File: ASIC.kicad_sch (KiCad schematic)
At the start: 66 parts, among them U10 BM1370_mode1, U11 MCP1824T-1202E/OT, U12 MCP1824T-0802E, U2 SN74AVC4T774, U8 25MHz, U9 BM1370_mode1

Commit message: lots of routing
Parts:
- removed U11: MCP1824T-1202E/OT, Package_TO_SOT_SMD:SOT-23-5, symbol bitaxe:MCP1824
- removed U12: MCP1824T-0802E, Package_TO_SOT_SMD:SOT-23-5, symbol bitaxe:MCP1824
- added R41: 38.3k, Resistor_SMD:R_0402_1005Metric, symbol Device:R_Small_US
- added R42, R44: 20k, Resistor_SMD:R_0402_1005Metric, symbol Device:R_Small_US
- added R43: 19.1k, Resistor_SMD:R_0402_1005Metric, symbol Device:R_Small_US
- added U11, U12: MCP1824, Package_TO_SOT_SMD:SOT-23-5, symbol bitaxe:MCP1824-ADJ
- A1: renamed from U9; value BM1370_mode1 -> BM1340_mode1; footprint bitaxe:BM1370 -> bitaxe:BM1340; symbol bitaxe:BM1370_mode1 -> bitaxe:BM1340_mode1
- A2: renamed from U10; value BM1370_mode1 -> BM1340_mode1; footprint bitaxe:BM1370 -> bitaxe:BM1340; symbol bitaxe:BM1370_mode1 -> bitaxe:BM1340_mode1
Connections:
- net 0V8: now also R43.2, U12.5 (VOUT)
- net 1V2: now also R41.2, U11.5 (VOUT)
- net 5V: now also U11.1 (VIN), U11.3 (EN), U12.1 (VIN), U12.3 (EN)
- net GND: now also R42.1, R44.1, U11.2 (GND), U12.2 (GND)
- new net: R41.1, R42.2, U11.4 (ADJ)
- new net: R43.1, R44.2, U12.4 (ADJ)
- no-connect marks 3 -> 1
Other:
- title: bitaxeGamma Turbo -> bitaxeNaja
- moved on the sheet: C89, C91, TP18, TP19

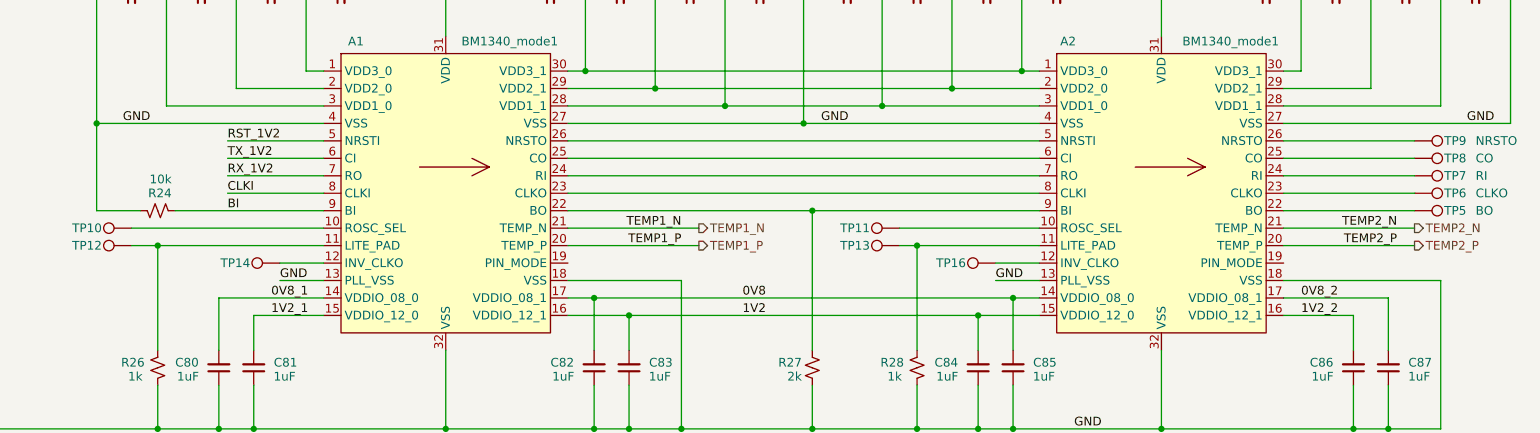
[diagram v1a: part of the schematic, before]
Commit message: placed and routed and DRC'd. updated TPS546 for 1.0V output.
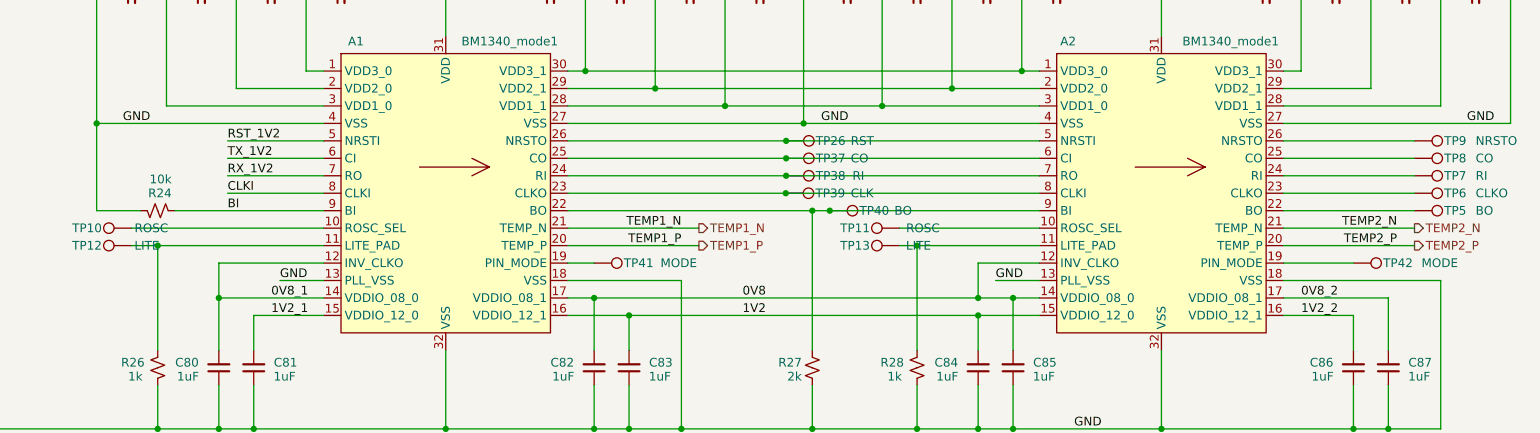
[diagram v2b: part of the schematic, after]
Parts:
- removed TP14, TP16: TestPoint, TestPoint:TestPoint_Pad_D1.0mm, symbol Connector:TestPoint
- added TP26: RST, bitaxe:TestPoint_Pad_1.0x0.4mm, symbol Connector:TestPoint
- added TP37: CO, bitaxe:TestPoint_Pad_1.0x0.4mm, symbol Connector:TestPoint
- added TP38: RI, bitaxe:TestPoint_Pad_1.0x0.4mm, symbol Connector:TestPoint
- added TP39: CLK, bitaxe:TestPoint_Pad_1.0x0.4mm, symbol Connector:TestPoint
- added TP40: BO, bitaxe:TestPoint_Pad_1.0x0.4mm, symbol Connector:TestPoint
- added TP41, TP42: MODE, bitaxe:TestPoint_Pad_1.0x0.4mm, symbol Connector:TestPoint
- R41: DK (none) -> YAG3141CT-ND; PARTNO (none) -> RC0402FR-0738K3L
- R42, R44: DK (none) -> 311-20.0KLRCT-ND; PARTNO (none) -> RC0402FR-0720KL
- R43: DK (none) -> 311-19.1KLRCT-ND; PARTNO (none) -> RC0402FR-0719K1L
- TP10, TP11: value TestPoint -> ROSC; footprint TestPoint:TestPoint_Pad_D1.0mm -> bitaxe:TestPoint_Pad_1.0x0.4mm
- TP12, TP13: value TestPoint -> LITE; footprint TestPoint:TestPoint_Pad_D1.0mm -> bitaxe:TestPoint_Pad_1.0x0.4mm
- TP5, TP6, TP7, TP8, TP9: footprint TestPoint:TestPoint_Pad_D1.0mm -> bitaxe:TestPoint_Pad_1.0x0.4mm
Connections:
- net 0V8: now also A2.12 (INV_CLKO)
- net 0V8_1: now also A1.12 (INV_CLKO)
- net at A1.19 (PIN_MODE): now also TP41.1
- net at A1.22 (BO), A2.9 (BI), R27.2: now also TP40.1
- net at A1.23 (CLKO), A2.8 (CLKI): now also TP39.1
- net at A1.24 (RI), A2.7 (RO): now also TP38.1
- net at A1.25 (CO), A2.6 (CI): now also TP37.1
- net at A1.26 (NRSTO), A2.5 (NRSTI): now also TP26.1
- net at A2.19 (PIN_MODE): now also TP42.1

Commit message: update to KiCad 10
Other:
- company: (none) -> bitaxeorg

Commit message: switched to single phase TPS546D24 and put the ASICs in series.
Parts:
- removed R41: 38.3k, Resistor_SMD:R_0402_1005Metric, symbol Device:R_Small_US
- removed R42, R44: 20k, Resistor_SMD:R_0402_1005Metric, symbol Device:R_Small_US
- removed R43: 19.1k, Resistor_SMD:R_0402_1005Metric, symbol Device:R_Small_US
- removed TP37: CO, bitaxe:TestPoint_Pad_1.0x0.4mm, symbol Connector:TestPoint
- removed TP38: RI, bitaxe:TestPoint_Pad_1.0x0.4mm, symbol Connector:TestPoint
- removed TP39: CLK, bitaxe:TestPoint_Pad_1.0x0.4mm, symbol Connector:TestPoint
- removed TP40: BO, bitaxe:TestPoint_Pad_1.0x0.4mm, symbol Connector:TestPoint
- removed U11, U12: MCP1824, Package_TO_SOT_SMD:SOT-23-5, symbol bitaxe:MCP1824-ADJ
- added C63, C96, C97, C98: 1uF, Capacitor_SMD:C_0402_1005Metric, symbol Device:C_Small
- added R38: 1k, Resistor_SMD:R_0402_1005Metric, symbol Device:R_Small_US
- added TP17: BO, bitaxe:TestPoint_Pad_1.0x0.4mm, symbol Connector:TestPoint
- added TP22: CO, bitaxe:TestPoint_Pad_1.0x0.4mm, symbol Connector:TestPoint
- added TP23: NRSTO, bitaxe:TestPoint_Pad_1.0x0.4mm, symbol Connector:TestPoint
- added TP24, TP27: GND, bitaxe:TestPoint_Pad_D1.0mm, symbol Connector:TestPoint
- added TP25, TP28: 0V8, bitaxe:TestPoint_Pad_D1.0mm, symbol Connector:TestPoint
- added TP30: 1V2, bitaxe:TestPoint_Pad_D1.0mm, symbol Connector:TestPoint
- added U10, U12: TLV77308PDBVR, Package_TO_SOT_SMD:SOT-23-5, symbol Regulator_Linear:TLV73312PDBV
- added U11, U14: TLV77312PDBVR, Package_TO_SOT_SMD:SOT-23-5, symbol Regulator_Linear:TLV73312PDBV
- A2: symbol bitaxe:BM1340_mode1 -> bitaxe:BM1340_mode0
- C88, C89, C90, C91: LCSC (none) -> C52923
- TP18: value 1V2 -> CLKO; footprint TestPoint:TestPoint_Pad_D1.5mm -> bitaxe:TestPoint_Pad_1.0x0.4mm
- TP19: value 0V8 -> RI; footprint TestPoint:TestPoint_Pad_D1.5mm -> bitaxe:TestPoint_Pad_1.0x0.4mm
- TP26: value RST -> 1V2; footprint bitaxe:TestPoint_Pad_1.0x0.4mm -> bitaxe:TestPoint_Pad_D1.0mm
- TP5: value BO -> BI
- TP6: value CLKO -> CLKI
- TP7: value RI -> RO
- TP8: value CO -> CI
- TP9: value NRSTO -> NRSTI
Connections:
- net 0V8_2 is gone; now on net 0V8_1: A2.17 (VDDIO_08_1), C87.2
- net 1V2_2 is gone; now on net 1V2_1: A2.16 (VDDIO_12_1), C86.2
- net 0V8_1: now also C97.2, TP28.1, U12.5 (OUT); no longer A1.12 (INV_CLKO), A1.14 (VDDIO_08_0), C80.2
- net 1V2: no longer A1.16 (VDDIO_12_1), A2.15 (VDDIO_12_0), C51.1, C53.1, C83.2, C84.2, C89.2, TP18.1, U2.16 (VCCA), U8.1 (EN), U8.4 (VIN)
- net 1V2_1: now also C98.2, R38.2, TP30.1, U14.5 (OUT); no longer A1.15 (VDDIO_12_0), C81.2
- net 5V: no longer C88.2, C90.2
- net GND: now also C63.1, TP24.1, U10.2 (GND), U11.2 (GND); no longer A1.27 (VSS), A2.13 (PLL_VSS), A2.18 (VSS), A2.27 (VSS), A2.32 (VSS), A2.4 (VSS), C58.2, C59.2, C60.2, C61.2, C62.2, C71.2, C72.1, C79.2, C84.1, C85.1, C86.1, C87.1, C91.1, R28.1
- net Level Shifter/BI: now reaches A1.22 (BO), R27.2
- net Level Shifter/BI: now also TP17.1; no longer A2.9 (BI)
- net at A2.8 (CO): no longer A1.23 (CLKO)
- net at A2.7 (RI): now also R38.1; no longer A1.24 (RI)
- net at A2.6 (CLKO): no longer A1.25 (CO)
- net at A1.28 (VDD1_1), C70.2, C71.1: no longer A2.3 (VDD1_0), C72.2, C73.1
- net at A1.29 (VDD2_1), C69.2, C70.1: no longer A2.2 (VDD2_0), C73.2, C74.1
- net at A1.30 (VDD3_1), C68.2, C69.1: no longer A2.1 (VDD3_0), C74.2, C75.1
- net Level Shifter/BO: now reaches TP5.1
- net Level Shifter/BO: now also A2.26 (BI); no longer A2.22 (BO)
- net Level Shifter/CLKO: now reaches TP6.1
- net Level Shifter/CLKO: now also A2.25 (CLKI); no longer A2.23 (CLKO)
- net Level Shifter/CO: now reaches TP8.1
- net Level Shifter/CO: now also A2.23 (CI); no longer A2.25 (CO)
- net GND_1: now reaches A2.19 (PIN_MODE), TP42.1
- net GND_1: now also A1.31 (VDD), A2.13 (PLL_VSS), A2.18 (VSS), A2.27 (VSS), A2.32 (VSS), A2.4 (VSS), C38.1, C54.1, C55.1, C56.1, C57.1, C58.2, C59.2, C60.2, C61.2, C62.2, C67.2, C68.1, C72.1, C79.2, C84.1, C85.1, C86.1, C87.1, C91.1, R28.1, C96.1, C97.1, C98.1, TP27.1, U12.2 (GND), U14.2 (GND)
- net Level Shifter/RI: now reaches A2.24 (RO), TP7.1
- net Level Shifter/NRSTO: now reaches TP9.1
- net Level Shifter/NRSTO: now also A2.22 (NRSTI); no longer A2.26 (NRSTO)
- removed net 0V8: A1.17 (VDDIO_08_1), A2.12 (INV_CLKO), A2.14 (VDDIO_08_0), C82.2, C85.2, C91.2, TP19.1
- net Vcore renamed VDD
- net VDD: no longer A1.31 (VDD), C38.1, C54.1, C55.1, C56.1, C57.1, C67.2, C68.1
- new net: A1.27 (VSS), C71.2
- new net: A2.3 (VDD1_0), C72.2, C73.1
- new net: A2.2 (VDD2_0), C73.2, C74.1
- new net: A2.1 (VDD3_0), C74.2, C75.1
- new net: A2.15 (VDDIO_12_0), C84.2
- new net: A2.12 (INV_CLKO), A2.14 (VDDIO_08_0), C85.2
- new net 0V8_0: A1.12 (INV_CLKO), A1.14 (VDDIO_08_0), A1.17 (VDDIO_08_1), C80.2, C82.2, C89.2, TP25.1, U10.5 (OUT)
- new net 1V2_0: A1.15 (VDDIO_12_0), A1.16 (VDDIO_12_1), C51.1, C53.1, C81.2, C83.2, C90.2, TP26.1, U11.5 (OUT), U2.16 (VCCA), U8.1 (EN), U8.4 (VIN)
- new net 5V_SWITCH: C63.2, C88.2, C91.2, C96.2, U10.1 (IN), U10.3 (EN), U11.1 (IN), U11.3 (EN), U12.1 (IN), U12.3 (EN), U14.1 (IN), U14.3 (EN)
- new net Level Shifter/CI: A1.25 (CO), TP22.1
- new net Level Shifter/CLKI: A1.23 (CLKO), TP18.1
- new net Level Shifter/NRSTI: A1.26 (NRSTO), TP23.1
- new net Level Shifter/RO: A1.24 (RI), TP19.1
- now unconnected: A2.5 (NRSTI)
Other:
- added sheet Level Shifter (level_shifter.kicad_sch)
- note added: "0.8V LDO"
- note added: "1.2V LDO"
- moved on the sheet: A1, A2, C38, C51, C52, C53, C54, C55, C56, C57, C58, C59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

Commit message: rough parts placement.
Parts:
- added C99: 0.1uF, Capacitor_SMD:C_0402_1005Metric, symbol Device:C_Small
- added R73: 0, Resistor_SMD:R_0402_1005Metric, symbol Device:R_US
- added TP31: CLKI, TestPoint:TestPoint_Pad_D1.0mm, symbol Connector:TestPoint
- added U15: 25MHz, bitaxe:SMD3225-4P, symbol bitaxe:oscillator
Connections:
- net 0V8_0: no longer A1.12 (INV_CLKO), A1.14 (VDDIO_08_0), C80.2
- net 1V2_0: no longer A1.15 (VDDIO_12_0), C81.2
- net 1V2_1: now also C99.1, U15.1 (EN), U15.4 (VIN)
- net GND: now also A1.27 (VSS), C71.2
- net GND_1: now also C99.2, U15.2 (GND)
- net Level Shifter/CLKO: now also R73.1
- new net: A1.12 (INV_CLKO), A1.14 (VDDIO_08_0), C80.2
- new net: A1.15 (VDDIO_12_0), C81.2
- new net CLKI_1: R73.2, TP31.1, U15.3 (OUT)
- no-connect marks 1 -> 5
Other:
- sheet Level Shifter ports: added GND_HI, GND_LO, VDD_HI; removed -VDD2, GND2, VDD2
- moved on the sheet: C38, C51, C52, C53, C54, C55, C56, C57, C58, C59, C60, C61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

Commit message: finished placing parts. lots of routing.
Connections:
- net 1V2 is gone; now on net 1V2_0: U2.7 (DIR3), U2.8 (DIR4)
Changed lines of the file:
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@@
-	(wire
-		(pts
-			(xy 62.23 105.41) (xy 74.93 105.41)
-		)
-		(stroke
-			(width 0)
-			(type default)
-		)
-	)
 	(wire
 		(pts
@@
 		)
 	)
-	(label "1V2"
+	(label "1V2_0"
 		(at 95.25 195.58 180)
 		(effects
@@
 		)
 	)
-	(label "5V"
-		(at 74.93 105.41 180)
-		(effects
-			(font
-				(size 1.27 1.27)
-			)
-			(justify right bottom)
-		)
-	)
-	(label "1V2"
+	(label "1V2_0"
 		(at 95.25 198.12 180)
 		(effects
@@
 		)
 	)
-	(hierarchical_label "5V"
+	(hierarchical_label "5V_SWITCH"
 		(shape input)
-		(at 62.23 105.41 180)
-		(effects
-			(font
+		(at 345.44 71.12 180)
+		(effects
+			(font

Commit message: finished routing
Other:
- moved on the sheet: C80, C81, C82, C83, C84, C85, R26, R27

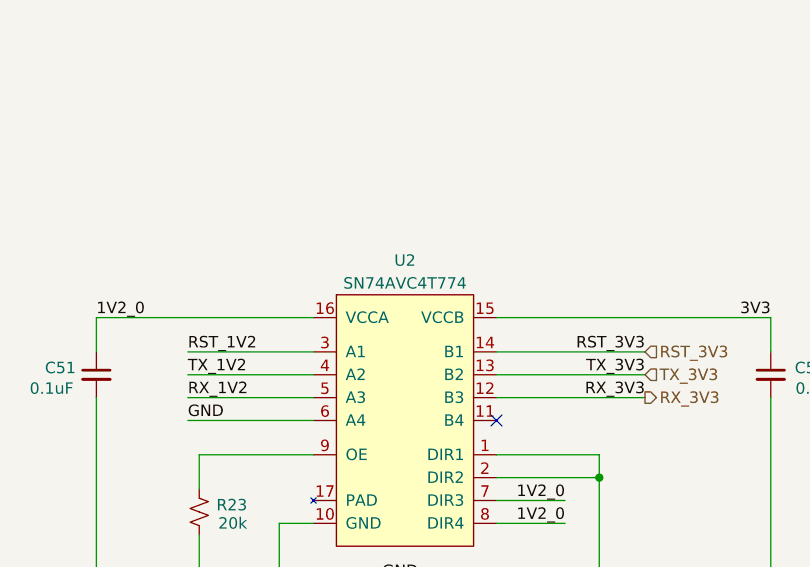
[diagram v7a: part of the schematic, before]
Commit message: AI BOM updates
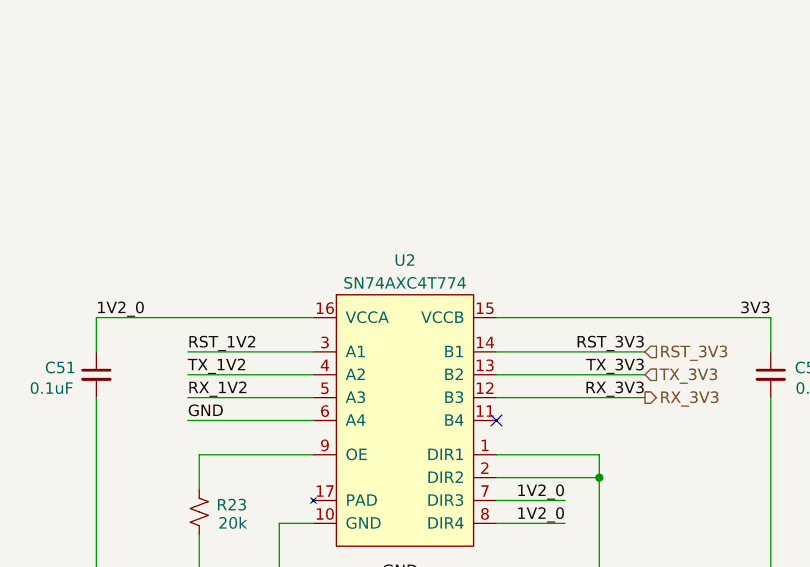
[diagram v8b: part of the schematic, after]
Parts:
- C38, C54, C55, C56, C57, C58, C59, C60, C61, C62: LCSC (none) -> C344022
- C63, C88, C89, C90, C91, C96, C97, C98: LCSC C52923 -> C2177690
- C64, C65, C66, C67, C68, C69, C70, C71, C72, C73, C74, C75, C76, C77, C78, C79, C80, C81, C82, C83, C84, C85, C86, C87: LCSC (none) -> C2177690
- R24: LCSC (none) -> C25744
- U2: value SN74AVC4T774 -> SN74AXC4T774
